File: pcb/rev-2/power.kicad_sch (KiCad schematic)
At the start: 36 parts, among them J1 12402012E212A, J3 B2B-PH-SM4-TB, SW1 EVQPUD02K, U1 NUF2042XV6T1G, U2 RT6160AWSC, U3 KTS1662EUW-TR, U4 BQ25150YFPR

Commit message: pcb: update
Mostly downsize several decoupling capacitors to save space
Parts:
- C11: value 10µF -> 22µF; manf# GRM188R61A106ME69D -> CL10A226MP8NUNE
- C12, C13, C15, C8, C9: value 4.7µF -> 10µF; footprint Capacitor_SMD:C_0603_1608Metric -> zeus-le:C_0402_1005Metric_Silkscreen_Clearance; manf# C1608X5R1E475K080AC -> CL05A106MP6NUN8
- C5: value 1µF -> 2.2µF; footprint Capacitor_SMD:C_0603_1608Metric -> zeus-le:C_0402_1005Metric_Silkscreen_Clearance; manf# CL10B105KP8NNNC -> GRM155R61A225ME01D
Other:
- moved on the sheet: C3, C5, U3

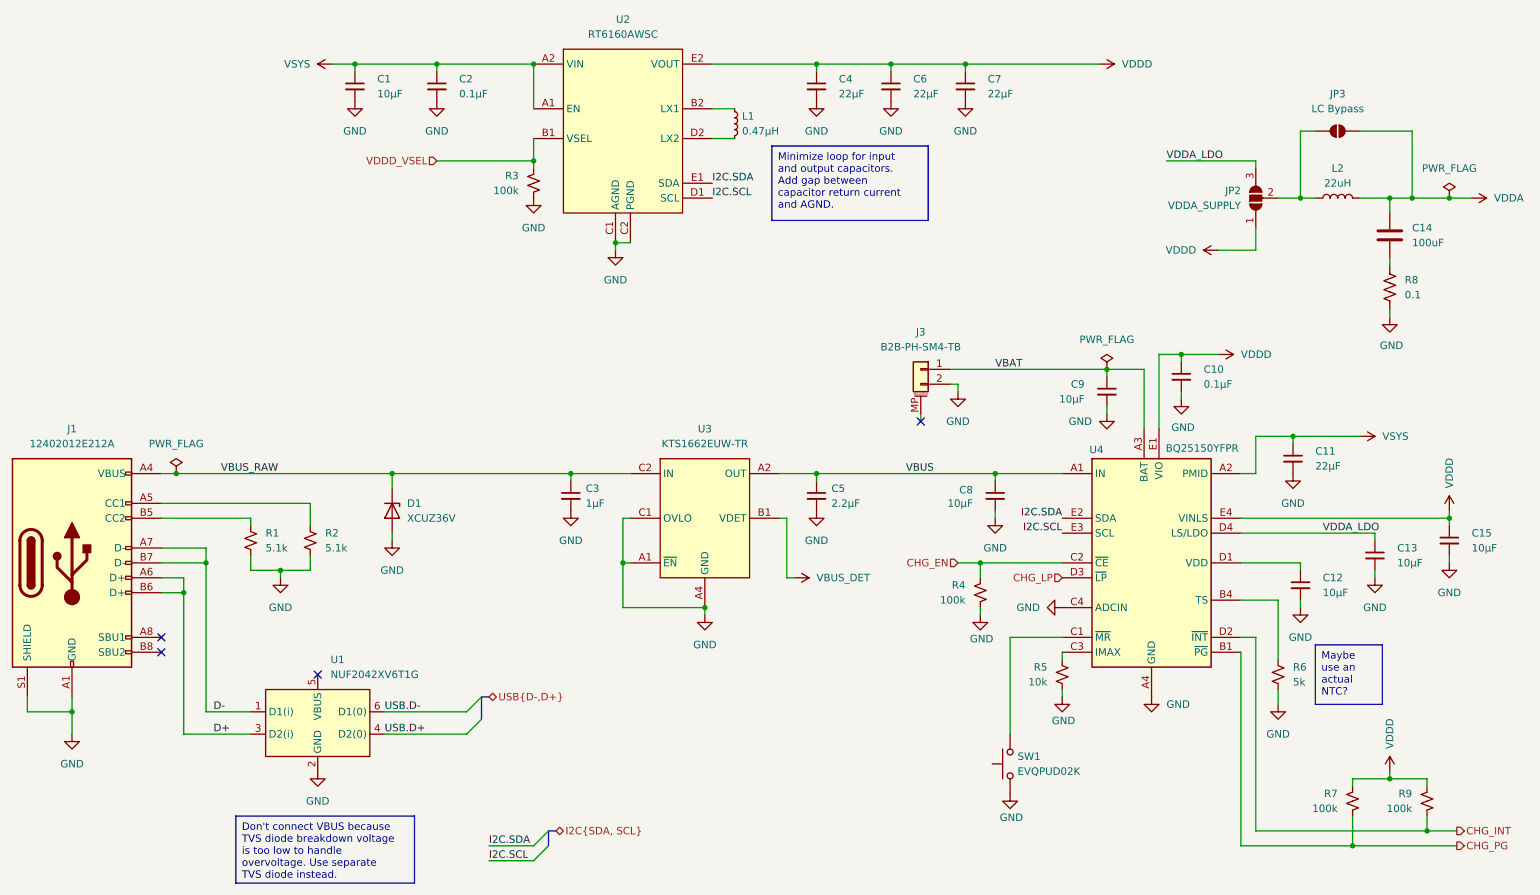
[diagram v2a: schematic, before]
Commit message: pcb: upgrade to KiCad 9.0
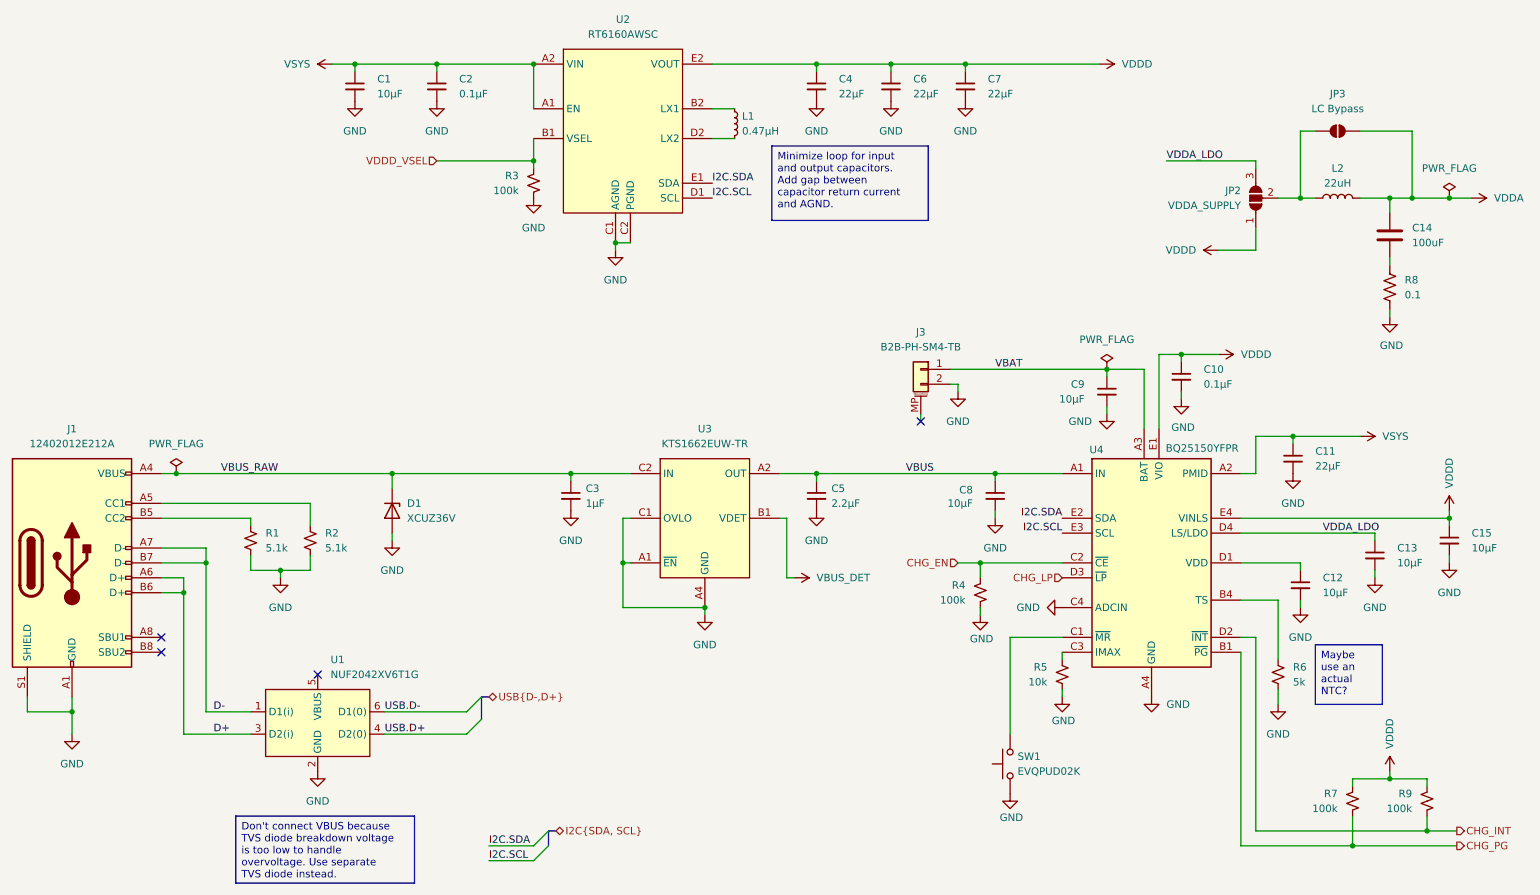
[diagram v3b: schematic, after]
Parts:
- JP3: manf# LC Bypass -> (none)
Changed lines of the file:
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@@
 (kicad_sch
-	(version 20231120)
+	(version 20250114)
 	(generator "eeschema")
-	(generator_version "8.0")
+	(generator_version "9.0")
 	(paper "A4")
 	(title_block
@@
 		(rev "2")
 	)
+	(text_box "Minimize loop for input and output capacitors. Add gap between capacitor return current and AGND."
+		(exclude_from_sim no)
+		(at 148.59 36.83 0)
+		(size 26.67 12.7)
+		(margins 0.9525 0.9525 0.9525 0.9525)
+		(stroke
+			(width 0)
+			(type default)
+		)
+		(fill
+			(type none)
+		)
+		(effects
+			(font
+				(size 1.27 1.27)
+			)
+			(justify left top)
+		)
+	)
+	(text_box "Don't connect VBUS because TVS diode breakdown voltage is too low to handle overvoltage. Use separate TVS diode instead."
+		(exclude_from_sim no)
+		(at 57.15 151.13 0)
+		(size 30.48 11.43)
+		(margins 0.9525 0.9525 0.9525 0.9525)
+		(stroke
+			(width 0)
+			(type default)
+		)
+		(fill
+			(type none)
+		)
+		(effects
+			(font
+				(size 1.27 1.27)
+			)
+			(justify left top)
+		)
+	)
+	(text_box "Maybe use an actual NTC?"
+		(exclude_from_sim no)
+		(at 241.3 121.92 0)
+		(size 11.43 10.16)
+		(margins 0.9525 0.9525 0.9525 0.9525)
+		(stroke
+			(width 0)
+			(type default)
+		)
+		(fill
+			(type none)
+		)
+		(effects
+			(font
+				(size 1.27 1.27)
+			)
+			(justify left top)
+		)
+	)
 	(junction
 		(at 52.07 107.95)
@@
 		)
 	)
-	(text_box "Minimize loop for input and output capacitors. Add gap between capacitor return current and AGND."
-		(exclude_from_sim no)
-		(at 148.59 36.83 0)
-		(size 26.67 12.7)
-		(stroke
-			(width 0)
-			(type default)
-		)
-		(fill
-			(type none)
-		)
-		(effects
-			(font
-				(size 1.27 1.27)
-			)
-			(justify left top)
-		)
-	)
-	(text_box "Don't connect VBUS because TVS diode breakdown voltage is too low to handle overvoltage. Use separate TVS diode instead."
-		(exclude_from_sim no)
-		(at 57.15 151.13 0)
-		(size 30.48 11.43)
-		(stroke
-			(width 0)
-			(type default)
-		)
-		(fill
-			(type none)
-		)
-		(effects
-			(font
-				(size 1.27 1.27)
-			)
-			(justify left top)
-		)
-	)
-	(text_box "Maybe use an actual NTC?"
-		(exclude_from_sim no)
-		(at 241.3 121.92 0)
-		(size 11.43 10.16)
-		(stroke
-			(width 0)
-			(type default)
-		)
-		(fill
-			(type none)
-		)
-		(effects
-			(font
-				(size 1.27 1.27)
-			)
-			(justify left top)
-		)
-	)
 	(label "VDDA_LDO"
 		(at 242.57 102.87 0)
-		(fields_autoplaced yes)
 		(effects
 			(font
@@
 	(label "I2C.SCL"
 		(at 198.12 102.87 180)
-		(fields_autoplaced yes)
 		(effects
 			(font
@@
 	(label "I2C.SCL"
 		(at 138.43 45.72 0)
-		(fields_autoplaced yes)
 		(effects
 			(font
@@
 	(label "VDDA_LDO"
 		(at 215.9 39.37 0)
-		(fields_autoplaced yes)
 		(effects
 			(font
@@
 	(label "I2C.SDA"
 		(at 138.43 43.18 0)
-		(fields_autoplaced yes)
 		(effects
 			(font
@@
 	(label "I2C.SDA"
 		(at 198.12 100.33 180)
-		(fields_autoplaced yes)
 		(effects
 			(font
@@
 	(label "I2C.SCL"
 		(at 100.33 158.75 0)
-		(fields_autoplaced yes)
 		(effects
 			(font
@@
 	(label "VBUS"
 		(at 171.45 92.71 0)
-		(fields_autoplaced yes)
 		(effects
 			(font
@@
 	(label "USB.D-"
 		(at 82.55 133.35 0)
-		(fields_autoplaced yes)
 		(effects
 			(font
@@
 	(label "VBUS_RAW"
 		(at 54.61 92.71 0)
-		(fields_autoplaced yes)
 		(effects
 			(font
@@
 	(label "USB.D+"
 		(at 82.55 137.16 0)
-		(fields_autoplaced yes)
 		(effects
 			(font
@@
 	(label "D+"
 		(at 53.34 137.16 0)
-		(fields_autoplaced yes)
 		(effects
 			(font
@@
 	(label "VBAT"
 		(at 186.69 74.93 0)
-		(fields_autoplaced yes)
 		(effects
 			(font
@@
 	(label "D-"
 		(at 53.34 133.35 0)
-		(fields_autoplaced yes)
 		(effects
 			(font
@@
 	(label "I2C.SDA"
 		(at 100.33 156.21 0)
-		(fields_autoplaced yes)
 		(effects
 			(font
@@
 		(shape output)
 		(at 265.43 153.67 0)
-		(fields_autoplaced yes)
 		(effects
 			(font
@@
 		(shape output)
 		(at 265.43 156.21 0)
-		(fields_autoplaced yes)
 		(effects
 			(font
@@
 		(shape bidirectional)
 		(at 100.33 130.81 0)
-		(fields_autoplaced yes)
 		(effects
 			(font
@@
 		(shape input)
 		(at 91.44 39.37 180)
-		(fields_autoplaced yes)
 		(effects
 			(font
@@
 		(shape input)
 		(at 198.12 110.49 180)
-		(fields_autoplaced yes)
 		(effects
 			(font
@@
 		(shape input)
 		(at 180.34 107.95 180)
-		(fields_autoplaced yes)
 		(effects
 			(font
@@
 		(shape bidirectional)
 		(at 111.76 153.67 0)
-		(fields_autoplaced yes)
 		(effects
 			(font
@@
 			(at 245.11 34.29 0)
 			(effects
-				(font
-					(size 1.27 1.27)
-				)
-				(hide yes)
-			)
-		)
-		(property "manf#" "LC Bypass"
-			(at 245.11 34.29 0)
-			(effects

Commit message: Update PCBs
* Update to KiCad 10
* Update footprint for nRF53 module based on 1.01 datasheet with
  actually readable mechanical drawing
* Add 3D model for production nRF53 module
* Remove overlapping silkscreen on rev-1 with production nRF53 module
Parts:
- D1: symbol Diode:ZPYxx -> Device:D_Zener
- J3: mouser# (none) -> 306-B2BPHSM4TBLFSN
